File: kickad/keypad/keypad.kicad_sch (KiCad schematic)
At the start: 3 parts

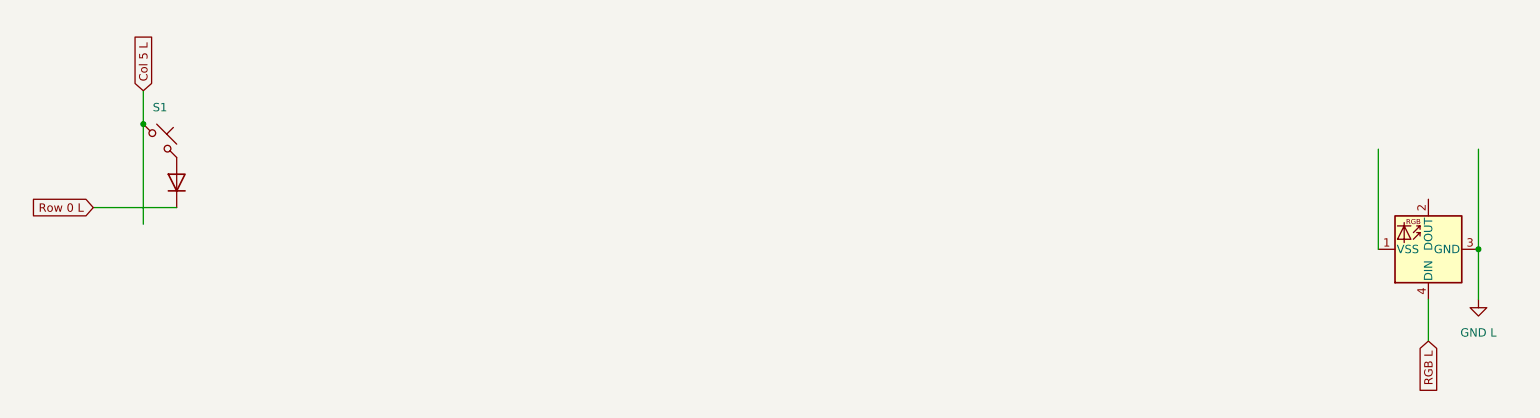
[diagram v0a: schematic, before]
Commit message: Reworking the keypad PCB
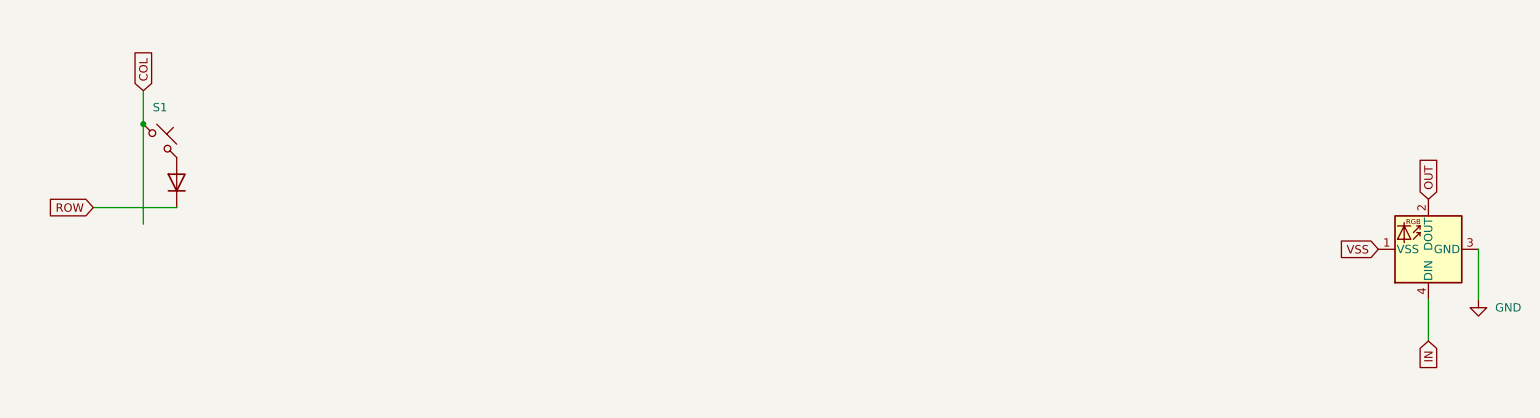
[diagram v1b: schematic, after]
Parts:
- renumbered D34 to D2
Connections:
- net VSS: now reaches D2.1 (VSS)
- net OUT: now reaches D2.2 (DOUT)
- net Col 5 L renamed COL
- net GND L renamed GND
- net RGB L renamed IN
- net Row 0 L renamed ROW
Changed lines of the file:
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@@
-		(color 0 0 0 0)
-	)
-	(junction
-		(at 356.87 57.15)
-		(diameter 0)
 		(color 0 0 0 0)
 	)
 	(wire
 		(pts
-			(xy 356.87 41.91) (xy 356.87 57.15)
+			(xy 146.05 50.8) (xy 158.75 50.8)
 		)
 		(stroke
@@
 	(wire
 		(pts
-			(xy 146.05 50.8) (xy 158.75 50.8)
+			(xy 153.67 33.02) (xy 153.67 38.1)
 		)
 		(stroke
@@
 	(wire
 		(pts
-			(xy 153.67 33.02) (xy 153.67 38.1)
+			(xy 349.25 71.12) (xy 349.25 64.77)
 		)
 		(stroke
@@
 	(wire
 		(pts
-			(xy 349.25 71.12) (xy 349.25 64.77)
+			(xy 153.67 38.1) (xy 153.67 53.34)
 		)
 		(stroke
@@
 	(wire
 		(pts
-			(xy 153.67 38.1) (xy 153.67 53.34)
+			(xy 356.87 64.77) (xy 356.87 57.15)
 		)
 		(stroke
@@
 		)
 	)
-	(wire
-		(pts
-			(xy 356.87 64.77) (xy 356.87 57.15)
-		)
-		(stroke
-			(width 0)
-			(type default)
-		)
-	)
-	(wire
-		(pts
-			(xy 341.63 41.91) (xy 341.63 57.15)
-		)
-		(stroke
-			(width 0)
-			(type default)
-		)
-	)
-	(global_label "Col 5 L"
+	(global_label "COL"
 		(shape input)
 		(at 153.67 33.02 90)
@@
 		)
 		(property "Intersheetrefs" "${INTERSHEET_REFS}"
-			(at 153.67 22.7778 90)
+			(at 153.67 26.4062 90)
 			(effects
 				(font
@@
 		)
 	)
-	(global_label "RGB L"
+	(global_label "VSS"
 		(shape input)
-		(at 349.25 71.12 270)
+		(at 341.63 57.15 180)
 		(fields_autoplaced yes)
 		(effects
@@
 		)
 		(property "Intersheetrefs" "${INTERSHEET_REFS}"
-			(at 349.25 79.9109 90)
+			(at 335.1372 57.15 0)
 			(effects
 				(font
@@
 		)
 	)
-	(global_label "Row 0 L"
+	(global_label "IN"
 		(shape input)
-		(at 146.05 50.8 180)
+		(at 349.25 71.12 270)
 		(fields_autoplaced yes)
 		(effects
@@
 		)
 		(property "Intersheetrefs" "${INTERSHEET_REFS}"
-			(at 135.1425 50.8 0)
+			(at 349.25 76.0405 90)
 			(effects
 				(font
@@
 				)
 				(justify right)
+				(hide yes)
+			)
+		)
+	)
+	(global_label "ROW"
+		(shape input)
+		(at 146.05 50.8 180)
+		(fields_autoplaced yes)
+		(effects
+			(font
+				(size 1.27 1.27)
+			)
+			(justify right)
+		)
+		(property "Intersheetrefs" "${INTERSHEET_REFS}"
+			(at 139.0129 50.8 0)
+			(effects
+				(font
+					(size 1.27 1.27)
+				)
+				(justify right)
+				(hide yes)
+			)
+		)
+	)
+	(global_label "OUT"
+		(shape input)
+		(at 349.25 49.53 90)
+		(fields_autoplaced yes)
+		(effects
+			(font
+				(size 1.27 1.27)
+			)
+			(justify left)
+		)
+		(property "Intersheetrefs" "${INTERSHEET_REFS}"
+			(at 349.25 42.9162 90)
+			(effects
+				(font
+					(size 1.27 1.27)
+				)
+				(justify left)
 				(hide yes)
 			)
@@
 			)
 		)
-		(property "Value" "GND L"
-			(at 356.87 69.85 0)
-			(effects
-				(font
-					(size 1.27 1.27)
-				)
+		(property "Value" "GND"
+			(at 359.41 66.0399 0)
+			(effects
+				(font
+					(size 1.27 1.27)
+				)
+				(justify left)
 			)
 		)
@@
 		(on_board yes)
 		(dnp no)
-		(property "Reference" "D34"
+		(property "Reference" "D2"
 			(at 343.916 45.72 90)
 			(effects
@@
 			(project "little-wing"
 				(path "/3a835e6f-a660-4b38-a102-87841cdd95ed"
-					(reference "D34")
+					(reference "D2")
 					(unit 1)
 				)
